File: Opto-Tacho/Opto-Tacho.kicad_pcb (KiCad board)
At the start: 2 copper layers, 20 x 20 mm, 1 part, among them J101 Interface

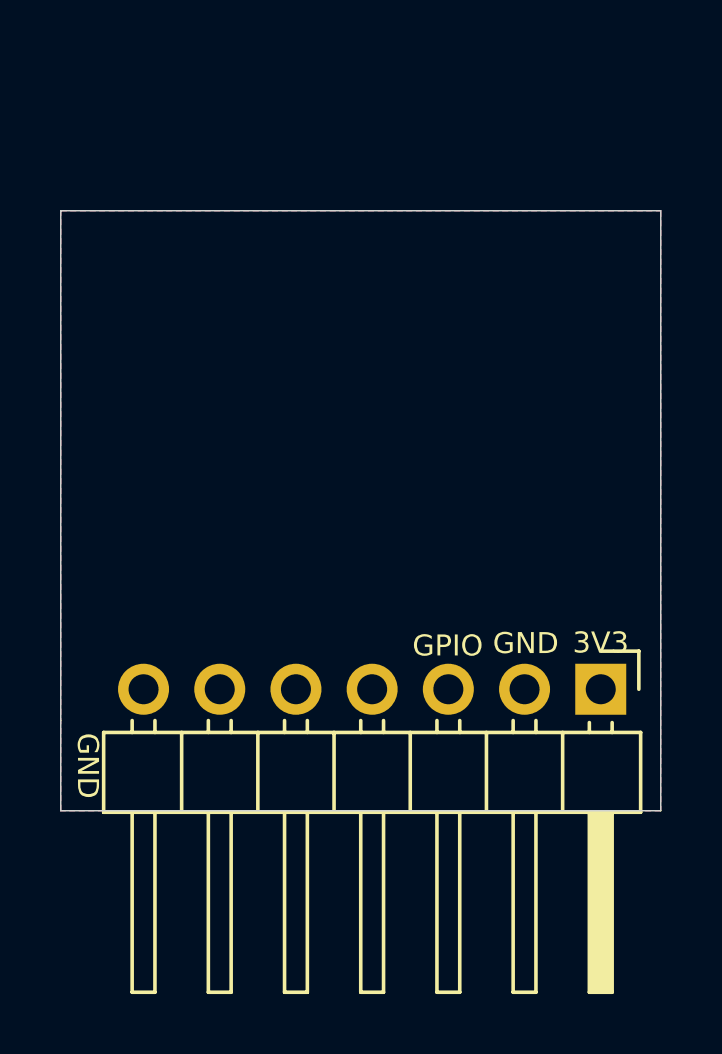
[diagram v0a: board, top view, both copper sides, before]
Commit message: Opto Tacho (Schmidtt),   Fixes to FET_Driver_Sense
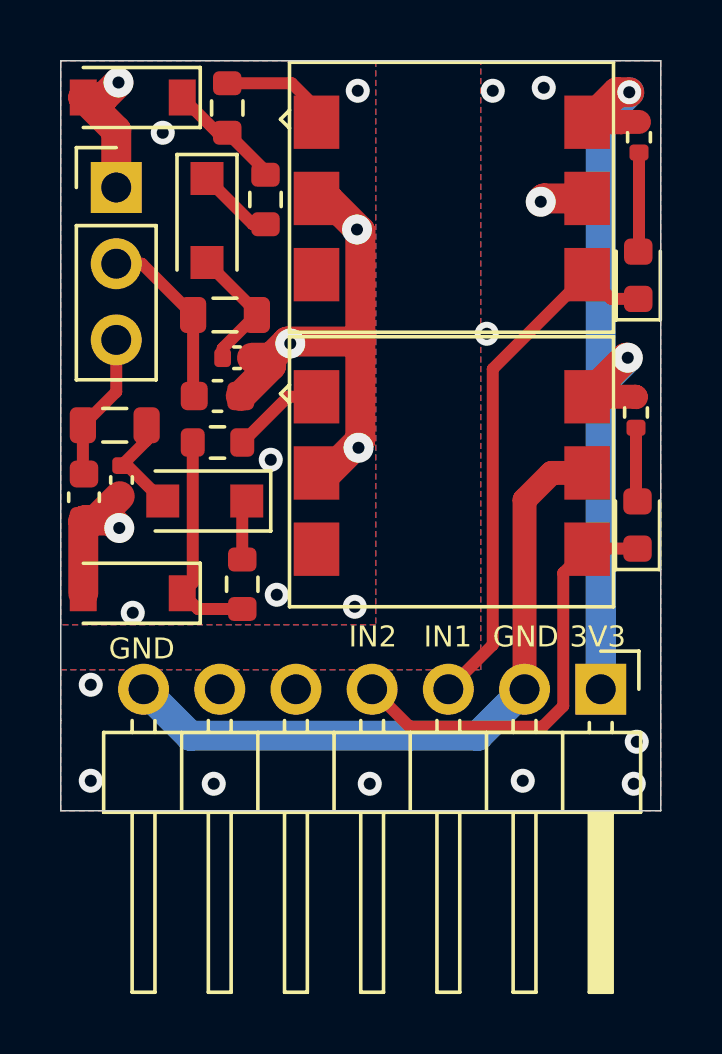
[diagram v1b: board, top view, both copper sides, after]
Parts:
- added C101: 33pF, Capacitor_SMD:C_0402_1005Metric, F.Cu at (125.9, 77.9)
- added C102: 33pF/50V, Capacitor_SMD:C_0603_1608Metric, F.Cu at (125.2, 79.2)
- added C103: 33pF, Capacitor_SMD:C_0402_1005Metric, F.Cu at (122.0, 82.0)
- added C104: 33pF/50V, Capacitor_SMD:C_0603_1608Metric, F.Cu at (120.8, 82.5)
- added D101: GREEN LED, LED_SMD:LED_0603_1608Metric, F.Cu at (139.2, 75.2)
- added D102: MM1Z4V7B, Diode_SMD:D_SOD-123, F.Cu at (122.4, 69.2)
- added D103: SM4007PL, Diode_SMD:D_SOD-123F, F.Cu at (124.9, 73.3)
- added D104: GREEN LED, LED_SMD:LED_0603_1608Metric, F.Cu at (139.2, 83.5)
- added D105: MM1Z4V7B, Diode_SMD:D_SOD-123, F.Cu at (122.4, 85.8)
- added D106: SM4007PL, Diode_SMD:D_SOD-123F, F.Cu at (124.8, 82.7)
- added FB101: GZ2012D101TF, Inductor_SMD:L_0805_2012Metric, F.Cu at (125.5, 76.5)
- added FB102: GZ2012D101TF, Inductor_SMD:L_0805_2012Metric, F.Cu at (121.8, 80.2)
- added J901: Conn_01x03, Connector_PinHeader_2.54mm:PinHeader_1x03_P2.54mm_Vertical, F.Cu at (121.8, 72.2)
- added R101: 1k, Resistor_SMD:R_0402_1005Metric, F.Cu at (139.3, 70.5)
- added R102: 330, Resistor_SMD:R_0603_1608Metric, F.Cu at (125.5, 69.6)
- added R103: 1k, Resistor_SMD:R_0603_1608Metric, F.Cu at (126.8, 72.6)
- added R104: 1k, Resistor_SMD:R_0402_1005Metric, F.Cu at (139.2, 79.7)
- added R105: 330, Resistor_SMD:R_0603_1608Metric, F.Cu at (125.2, 80.7)
- added R106: 1k, Resistor_SMD:R_0603_1608Metric, F.Cu at (126.0, 85.5)
- added U101: H11L1SR2M, yacht_hardware:SMT-6_6.4x8.5x2.54P, F.Cu at (140.5, 75.0)
- added U102: H11L1SR2M, yacht_hardware:SMT-6_6.4x8.5x2.54P, F.Cu at (140.5, 84.2)
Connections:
- J101 pad 1: (no net) -> +3V3
- J101 pad 3: (no net) -> /GPIO_1
- J101 pad 4: (no net) -> /GPIO_2
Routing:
- net +3V3: track 0.00 -> 38.8 mm, vias 0 -> 2
- net /ISO_GND: track 0.00 -> 26.4 mm, vias 0 -> 11
- net GND: track 0.00 -> 24.3 mm, vias 0 -> 11
- net /GPIO_1: track 0.00 -> 17.8 mm
- net /GPIO_2: track 0.00 -> 14.4 mm
- net Net-(D105-Pad1): track 0.00 -> 7.39 mm
- net /ISO_IN_1: track 0.00 -> 5.99 mm
- net /ISO_IN_2: track 0.00 -> 4.95 mm
- net Net-(C101-Pad1): track 0.00 -> 4.35 mm
- net Net-(D102-Pad1): track 0.00 -> 3.91 mm
- net Net-(R102-Pad2): track 0.00 -> 3.79 mm
- net Net-(C103-Pad1): track 0.00 -> 3.56 mm
- net Net-(D101-Pad2): track 0.00 -> 3.31 mm
- net Net-(R105-Pad2): track 0.00 -> 3.11 mm
- net Net-(D103-Pad1): track 0.00 -> 2.58 mm
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- added copper zone on B.Cu, net /ISO_GND
- added copper zone on F.Cu, net /ISO_GND
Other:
- board size 20 x 20 mm -> 20 x 25 mm
- board text added: "GND_ISO"
- board text added: "IN1"
- board text added: "IN2"
- board text added: "ISO_IN1"
- board text added: "ISO_IN2"
- board text removed: "GPIO"
- board text removed: "Hole here is for Single pin to support board edge if needed for connectors when Horizontal on SH-ESP32"

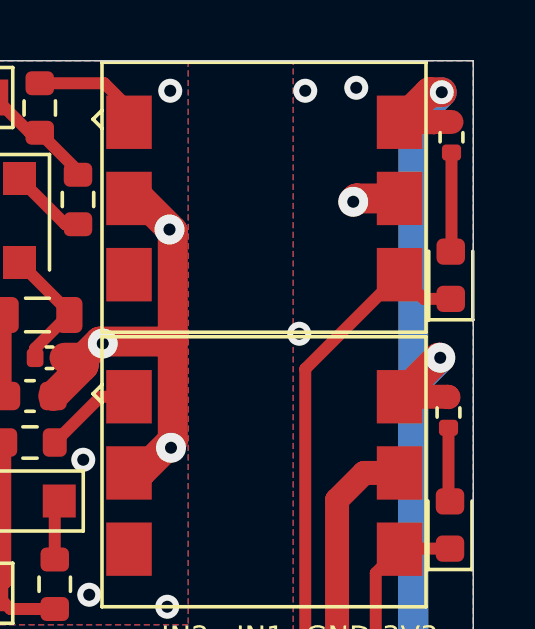
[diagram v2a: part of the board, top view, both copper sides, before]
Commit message: Fix Resistor sizes to all are 603
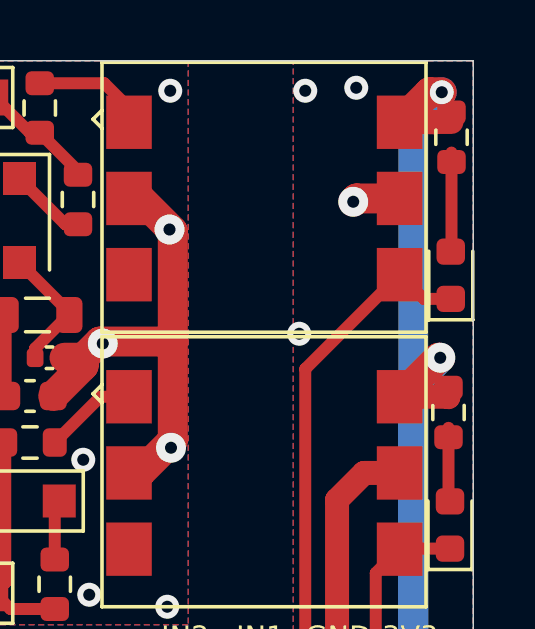
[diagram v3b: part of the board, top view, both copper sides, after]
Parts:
- R101, R104: footprint Resistor_SMD:R_0402_1005Metric -> Resistor_SMD:R_0603_1608Metric

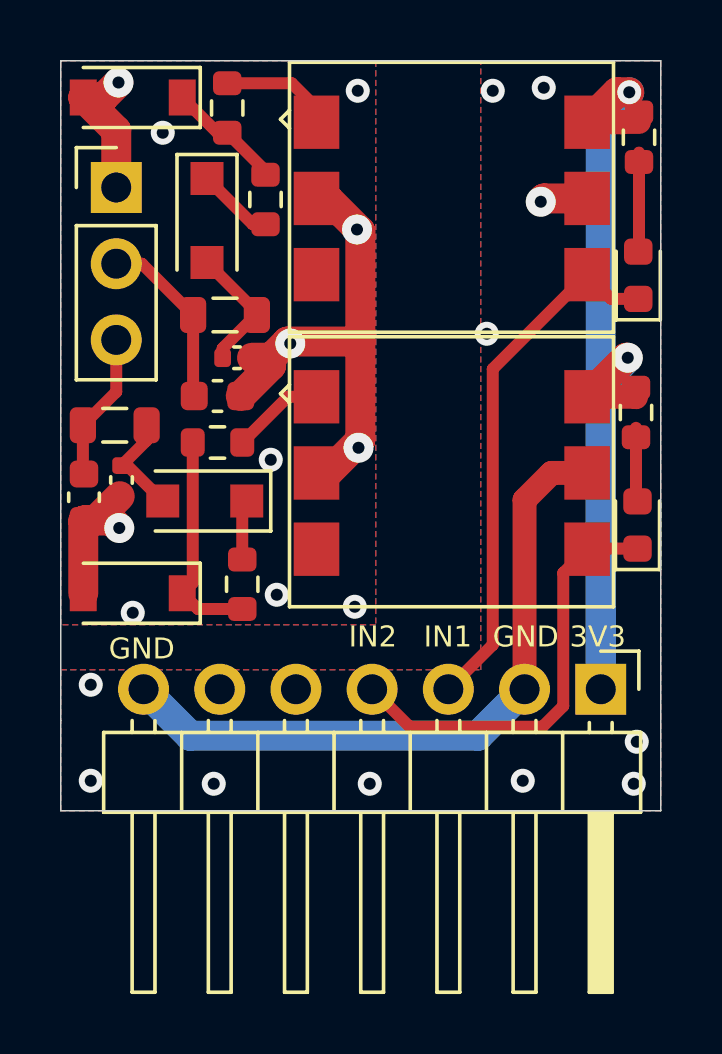
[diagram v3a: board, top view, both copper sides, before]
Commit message: Fix Footprint center for Opto
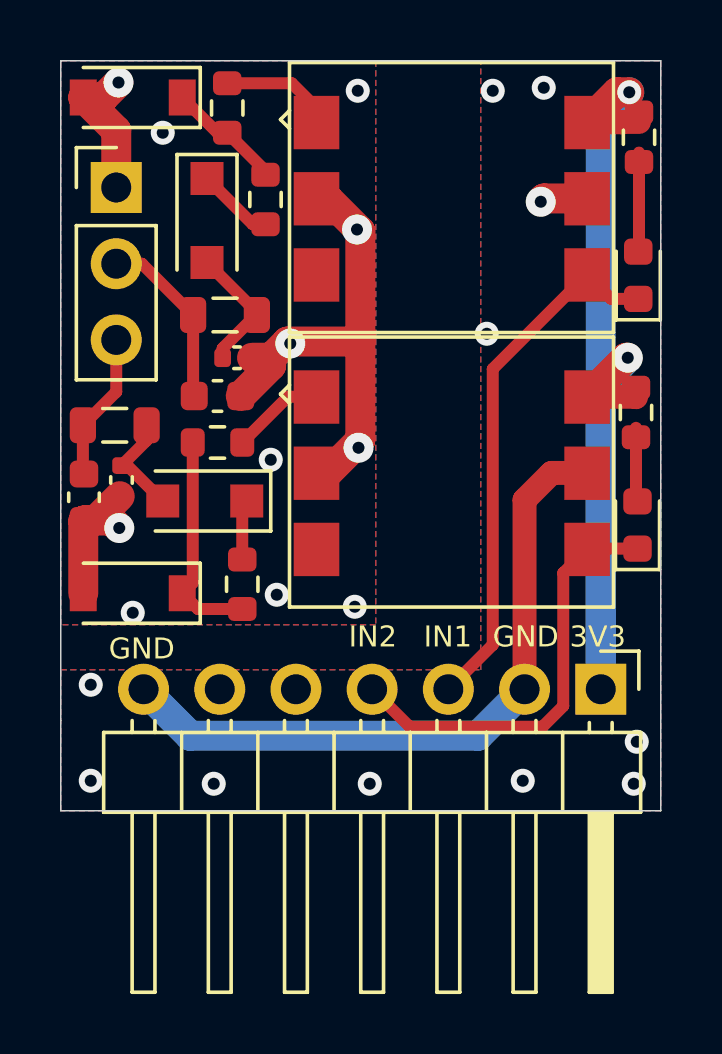
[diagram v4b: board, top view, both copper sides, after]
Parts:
- moved U101 7.94 mm to (133.0, 72.6)
- moved U102 7.94 mm to (133.0, 81.8)
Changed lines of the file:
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@@
     (add_net /GPIO_1)
     (add_net /GPIO_2)
-    (add_net /GPIO_3)
-    (add_net /GPIO_4)
     (add_net /ISO_GND)
     (add_net /ISO_IN_1)
@@
     (add_net "Net-(R102-Pad2)")
     (add_net "Net-(R105-Pad2)")
-    (add_net "Net-(U101-Pad3)")
-    (add_net "Net-(U102-Pad3)")
+  )
+  (module yacht_hardware:SMT-6_6.4x8.5x2.54P (layer F.Cu)
+    (at 132.975 81.75 270)
+    (fp_text reference U102 (at 0 0.5 90) (layer F.SilkS) hide
+      (effects (font (size 1 1) (thickness 0.15)))
+    )
+    (fp_text value H11L1SR2M (at 0 -0.5 90) (layer F.Fab) hide
+      (effects (font (size 1 1) (thickness 0.15)))
+    )
+    (fp_line (start 0.35 0) (end -0.31 0) (layer Dwgs.User) (width 0.01))
+    (fp_line (start 0 -0.2) (end 0 0.2) (layer Dwgs.User) (width 0.01))
+    (fp_line (start -4.54 5.35) (end 4.46 5.35) (layer F.CrtYd) (width 0.12))
+    (fp_line (start 4.46 5.35) (end 4.46 -5.45) (layer F.CrtYd) (width 0.12))
+    (fp_line (start 4.46 -5.45) (end -4.54 -5.45) (layer F.CrtYd) (width 0.12))
+    (fp_line (start -4.54 -5.45) (end -4.54 5.35) (layer F.CrtYd) (width 0.12))
+    (fp_line (start -4.54 5.35) (end 4.46 5.35) (layer F.SilkS) (width 0.12))
+    (fp_line (start 4.46 5.35) (end 4.46 -5.45) (layer F.SilkS) (width 0.12))
+    (fp_line (start 4.46 -5.45) (end -4.54 -5.45) (layer F.SilkS) (width 0.12))
+    (fp_line (start -4.54 -5.45) (end -4.54 5.35) (layer F.SilkS) (width 0.12))
+    (fp_line (start -2.94 5.35) (end -2.64 5.65) (layer F.SilkS) (width 0.12))
+    (fp_line (start -2.64 5.65) (end -2.34 5.35) (layer F.SilkS) (width 0.12))
+    (pad 1 smd rect (at -2.54 4.45 270) (size 1.78 1.52) (layers F.Cu F.Paste F.Mask)
+      (net 17 "Net-(R105-Pad2)"))
+    (pad 2 smd rect (at 0 4.45 270) (size 1.78 1.52) (layers F.Cu F.Paste F.Mask)
+      (net 2 /ISO_GND))
+    (pad 3 smd rect (at 2.54 4.45 270) (size 1.78 1.52) (layers F.Cu F.Paste F.Mask))
+    (pad 4 smd rect (at 2.54 -4.57 270) (size 1.78 1.52) (layers F.Cu F.Paste F.Mask)
+      (net 10 /GPIO_2))
+    (pad 5 smd rect (at 0 -4.57 270) (size 1.78 1.52) (layers F.Cu F.Paste F.Mask)
+      (net 1 GND))
+    (pad 6 smd rect (at -2.54 -4.57 270) (size 1.78 1.52) (layers F.Cu F.Paste F.Mask)
+      (net 11 +3V3))
+  )
+  (module yacht_hardware:SMT-6_6.4x8.5x2.54P (layer F.Cu)
+    (at 132.975 72.6 270)
+    (fp_text reference U101 (at 0 0.5 90) (layer F.SilkS) hide
+      (effects (font (size 1 1) (thickness 0.15)))
+    )
+    (fp_text value H11L1SR2M (at 0 -0.5 90) (layer F.Fab) hide
+      (effects (font (size 1 1) (thickness 0.15)))
+    )
+    (fp_line (start 0.35 0) (end -0.31 0) (layer Dwgs.User) (width 0.01))
+    (fp_line (start 0 -0.2) (end 0 0.2) (layer Dwgs.User) (width 0.01))
+    (fp_line (start -4.54 5.35) (end 4.46 5.35) (layer F.CrtYd) (width 0.12))
+    (fp_line (start 4.46 5.35) (end 4.46 -5.45) (layer F.CrtYd) (width 0.12))
+    (fp_line (start 4.46 -5.45) (end -4.54 -5.45) (layer F.CrtYd) (width 0.12))
+    (fp_line (start -4.54 -5.45) (end -4.54 5.35) (layer F.CrtYd) (width 0.12))
+    (fp_line (start -4.54 5.35) (end 4.46 5.35) (layer F.SilkS) (width 0.12))
+    (fp_line (start 4.46 5.35) (end 4.46 -5.45) (layer F.SilkS) (width 0.12))
+    (fp_line (start 4.46 -5.45) (end -4.54 -5.45) (layer F.SilkS) (width 0.12))
+    (fp_line (start -4.54 -5.45) (end -4.54 5.35) (layer F.SilkS) (width 0.12))
+    (fp_line (start -2.94 5.35) (end -2.64 5.65) (layer F.SilkS) (width 0.12))
+    (fp_line (start -2.64 5.65) (end -2.34 5.35) (layer F.SilkS) (width 0.12))
+    (pad 1 smd rect (at -2.54 4.45 270) (size 1.78 1.52) (layers F.Cu F.Paste F.Mask)
+      (net 13 "Net-(R102-Pad2)"))
+    (pad 2 smd rect (at 0 4.45 270) (size 1.78 1.52) (layers F.Cu F.Paste F.Mask)
+      (net 2 /ISO_GND))
+    (pad 3 smd rect (at 2.54 4.45 270) (size 1.78 1.52) (layers F.Cu F.Paste F.Mask))
+    (pad 4 smd rect (at 2.54 -4.57 270) (size 1.78 1.52) (layers F.Cu F.Paste F.Mask)
+      (net 6 /GPIO_1))
+    (pad 5 smd rect (at 0 -4.57 270) (size 1.78 1.52) (layers F.Cu F.Paste F.Mask)
+      (net 1 GND))
+    (pad 6 smd rect (at -2.54 -4.57 270) (size 1.78 1.52) (layers F.Cu F.Paste F.Mask)
+      (net 11 +3V3))
   )
   (module Resistor_SMD:R_0603_1608Metric (layer F.Cu)
@@
     (fp_text value 1k (at 0 1.43 90) (layer F.Fab) hide
       (effects (font (size 1 1) (thickness 0.15)))
-    )
-    (fp_text user %R (at 0 0 90) (layer F.Fab) hide
-      (effects (font (size 0.4 0.4) (thickness 0.06)))
     )
     (fp_line (start -0.8 0.4125) (end -0.8 -0.4125) (layer F.Fab) (width 0.1))
@@
     (fp_line (start 1.48 -0.73) (end 1.48 0.73) (layer F.CrtYd) (width 0.05))
     (fp_line (start 1.48 0.73) (end -1.48 0.73) (layer F.CrtYd) (width 0.05))
+    (fp_text user %R (at 0 0 90) (layer F.Fab) hide
+      (effects (font (size 0.4 0.4) (thickness 0.06)))
+    )
     (pad 2 smd roundrect (at 0.825 0 270) (size 0.8 0.95) (layers F.Cu F.Paste F.Mask) (roundrect_rratio 0.25)
       (net 5 "Net-(D101-Pad2)"))
@@
     (fp_text value 1k (at 0 1.43 90) (layer F.Fab) hide
       (effects (font (size 1 1) (thickness 0.15)))
-    )
-    (fp_text user %R (at 0 0 90) (layer F.Fab) hide
-      (effects (font (size 0.4 0.4) (thickness 0.06)))
     )
     (fp_line (start -0.8 0.4125) (end -0.8 -0.4125) (layer F.Fab) (width 0.1))
@@
     (fp_line (start 1.48 -0.73) (end 1.48 0.73) (layer F.CrtYd) (width 0.05))
     (fp_line (start 1.48 0.73) (end -1.48 0.73) (layer F.CrtYd) (width 0.05))
+    (fp_text user %R (at 0 0 90) (layer F.Fab) hide
+      (effects (font (size 0.4 0.4) (thickness 0.06)))
+    )
     (pad 2 smd roundrect (at 0.825 0 270) (size 0.8 0.95) (layers F.Cu F.Paste F.Mask) (roundrect_rratio 0.25)
       (net 9 "Net-(D104-Pad2)"))
@@
       (rotate (xyz 0 0 0))
     )
-  )
-  (module yacht_hardware:SMT-6_6.4x8.5x2.54P (layer F.Cu)
-    (at 140.525 84.2 270)
-    (attr smd)
-    (fp_text reference U102 (at 0 0.5 90) (layer F.SilkS) hide
-      (effects (font (size 1 1) (thickness 0.15)))
-    )
-    (fp_text value H11L1SR2M (at 0 -0.5 90) (layer F.Fab) hide
-      (effects (font (size 1 1) (thickness 0.15)))
-    )
-    (fp_line (start -7 12.9) (end 2 12.9) (layer F.CrtYd) (width 0.12))
-    (fp_line (start 2 12.9) (end 2 2.1) (layer F.CrtYd) (width 0.12))
-    (fp_line (start 2 2.1) (end -7 2.1) (layer F.CrtYd) (width 0.12))
-    (fp_line (start -7 2.1) (end -7 12.9) (layer F.CrtYd) (width 0.12))
-    (fp_line (start -7 12.9) (end 2 12.9) (layer F.SilkS) (width 0.12))
-    (fp_line (start 2 12.9) (end 2 2.1) (layer F.SilkS) (width 0.12))
-    (fp_line (start 2 2.1) (end -7 2.1) (layer F.SilkS) (width 0.12))
-    (fp_line (start -7 2.1) (end -7 12.9) (layer F.SilkS) (width 0.12))
-    (fp_line (start -5.4 12.9) (end -5.1 13.2) (layer F.SilkS) (width 0.12))
-    (fp_line (start -5.1 13.2) (end -4.8 12.9) (layer F.SilkS) (width 0.12))
-    (pad 6 smd rect (at -5 2.98 270) (size 1.78 1.52) (layers F.Cu F.Paste F.Mask)
-      (net 11 +3V3))
-    (pad 5 smd rect (at -2.46 2.98 270) (size 1.78 1.52) (layers F.Cu F.Paste F.Mask)
-      (net 1 GND))
-    (pad 4 smd rect (at 0.08 2.98 270) (size 1.78 1.52) (layers F.Cu F.Paste F.Mask)
-      (net 10 /GPIO_2))
-    (pad 3 smd rect (at 0.08 12 270) (size 1.78 1.52) (layers F.Cu F.Paste F.Mask))
-    (pad 2 smd rect (at -2.46 12 270) (size 1.78 1.52) (layers F.Cu F.Paste F.Mask)
-      (net 2 /ISO_GND))
-    (pad 1 smd rect (at -5 12 270) (size 1.78 1.52) (layers F.Cu F.Paste F.Mask)
-      (net 17 "Net-(R105-Pad2)"))
   )
   (module Resistor_SMD:R_0603_1608Metric (layer F.Cu)
@@
     )
   )
-  (module yacht_hardware:SMT-6_6.4x8.5x2.54P (layer F.Cu)
-    (at 140.525 75.05 270)
-    (attr smd)
-    (fp_text reference U101 (at 0 0.5 90) (layer F.SilkS) hide
-      (effects (font (size 1 1) (thickness 0.15)))
-    )
-    (fp_text value H11L1SR2M (at 0 -0.5 90) (layer F.Fab) hide
-      (effects (font (size 1 1) (thickness 0.15)))
-    )
-    (fp_line (start -7 12.9) (end 2 12.9) (layer F.CrtYd) (width 0.12))
-    (fp_line (start 2 12.9) (end 2 2.1) (layer F.CrtYd) (width 0.12))
-    (fp_line (start 2 2.1) (end -7 2.1) (layer F.CrtYd) (width 0.12))
-    (fp_line (start -7 2.1) (end -7 12.9) (layer F.CrtYd) (width 0.12))
-    (fp_line (start -7 12.9) (end 2 12.9) (layer F.SilkS) (width 0.12))
-    (fp_line (start 2 12.9) (end 2 2.1) (layer F.SilkS) (width 0.12))
-    (fp_line (start 2 2.1) (end -7 2.1) (layer F.SilkS) (width 0.12))
-    (fp_line (start -7 2.1) (end -7 12.9) (layer F.SilkS) (width 0.12))
-    (fp_line (start -5.4 12.9) (end -5.1 13.2) (layer F.SilkS) (width 0.12))
-    (fp_line (start -5.1 13.2) (end -4.8 12.9) (layer F.SilkS) (width 0.12))
-    (pad 6 smd rect (at -5 2.98 270) (size 1.78 1.52) (layers F.Cu F.Paste F.Mask)
-      (net 11 +3V3))
-    (pad 5 smd rect (at -2.46 2.98 270) (size 1.78 1.52) (layers F.Cu F.Paste F.Mask)
-      (net 1 GND))
-    (pad 4 smd rect (at 0.08 2.98 270) (size 1.78 1.52) (layers F.Cu F.Paste F.Mask)
-      (net 6 /GPIO_1))
-    (pad 3 smd rect (at 0.08 12 270) (size 1.78 1.52) (layers F.Cu F.Paste F.Mask))
-    (pad 2 smd rect (at -2.46 12 270) (size 1.78 1.52) (layers F.Cu F.Paste F.Mask)
-      (net 2 /ISO_GND))
-    (pad 1 smd rect (at -5 12 270) (size 1.78 1.52) (layers F.Cu F.Paste F.Mask)
-      (net 13 "Net-(R102-Pad2)"))
-  )
   (module Resistor_SMD:R_0603_1608Metric (layer F.Cu)
